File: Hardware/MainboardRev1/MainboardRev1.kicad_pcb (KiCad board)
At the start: 4 copper layers, 92 x 92 mm, 224 parts, among them J1 BACKUP_BATT: 1586038-2, J10 Switch_1, J11 Switch_3, J12 Switch_2, J13 Switch_4, J14 Buzzer, J15 Strobe, J2 MAIN_BATT: 1586038-2, J3 Servo_Control, J4 EMATCH_1: 1586038-2, J5 EMATCH_2: 1586038-2, J6 Stratologger_PWR: 1586038-2, J7 Stratologger_DATA, J8 U.FL-R-SMT-1(10), J9 0733910320 [915MHz SMA], Q1 SSM3J328R, Q10 SSM3J328R, Q11 NTR4003, Q12 NTR4003, Q13 NTR4003, Q14 NTR4003, Q15 SSM3J328R, Q16 NTR4003, Q17 SSM3J328R, Q18 SSM3J328R, Q19 NTR4003, Q2 SSM3J328R, Q20 NTR4003, Q21 SIS612EDNT-T1-GE3, Q22 SIS612EDNT-T1-GE3, Q23 NTR4003, Q24 NTR4003, Q25 NTR4003, Q26 SSM3J328R, Q27 NTR4003, Q28 SSM3J328R, Q29 SSM3J328R, Q3 SSM3J328R, Q30 NTR4003, Q31 NTR4003, Q4 SSM3J328R, Q5 NTR4003, Q6 NTR4003, Q7 NTR4003, Q8 SSM3J328R, Q9 NTR4003, SW1 EG2201A [DPDT], U1 LT6703-3, U10 LTC4358, U11 Teensy3.6, U12 ABPMANN030PG2A3, U13 LSM9DS1, U14 LIS331HH, U15 BME280, U16 CCS811, U17 ublox_max-m8q, U18 RFM69HCW, U2 LTC3605, U3 LTC4358, U4 LTC4358, U5 LDL1117S50R, U6 LDL1117S33R, U7 LTC2992, U8 LDL1117S33R, U9 LTC2992

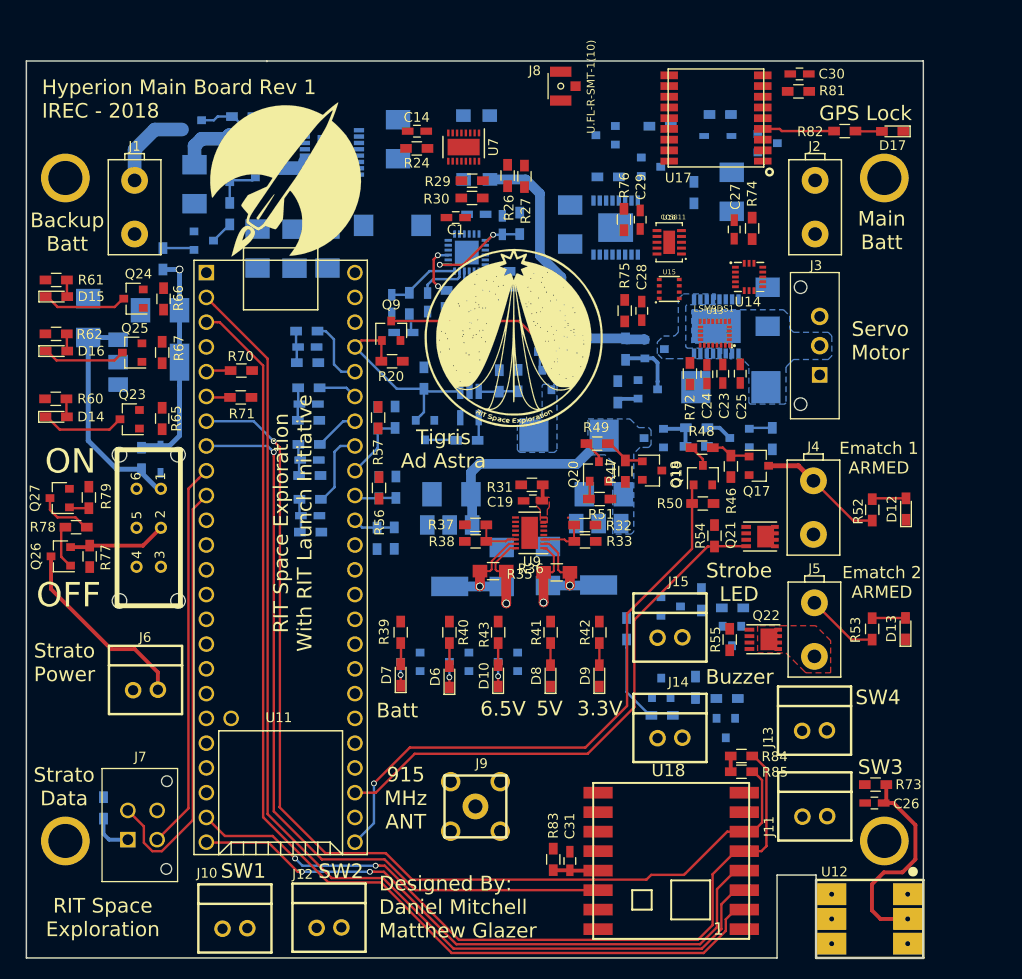
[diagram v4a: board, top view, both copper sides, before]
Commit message: committing progress, estimating the board is approx 1/3 routed
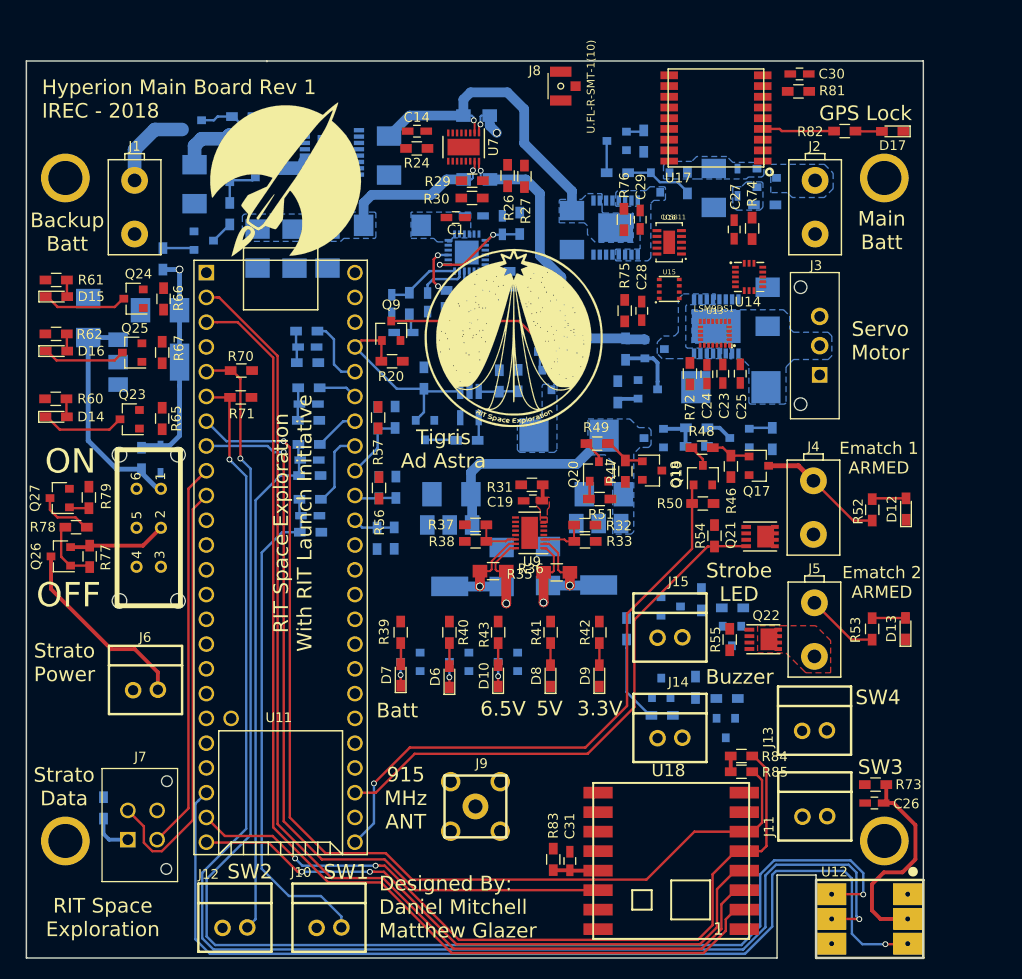
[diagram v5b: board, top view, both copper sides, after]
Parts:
- moved R2 10.3 mm to (125.7, 64.8)
- moved J10 9.65 mm to (81.0, 138.9)
- moved J12 9.65 mm to (71.4, 138.9)
- moved D2 5.16 mm to (122.9, 62.4), turned to 90 degrees
- moved Q2 3.56 mm to (125.9, 62.0)
- moved R13 2.27 mm to (113.3, 58.2), turned to 270 degrees
- moved C11 1.91 mm to (87.2, 59.7)
- moved C3 1.88 mm to (120.5, 63.0)
- moved Q4 1.86 mm to (115.0, 62.5), turned to 270 degrees
- moved Q6 1.28 mm to (110.5, 58.2)
- moved R8 1.22 mm to (117.8, 62.5)
- moved R11 1.04 mm to (110.6, 61.5)
- moved C13 0.59 mm to (106.0, 67.3)
- moved C6 0.31 mm to (95.9, 65.9)
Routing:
- net SENSORS_SCL: track 2.54 -> 143.8 mm, vias 0 -> 2
- net SENSORS_SDA: track 2.47 -> 142.9 mm, vias 0 -> 2
- net INT_PRESSURE: track 0.00 -> 102.3 mm, vias 0 -> 1
- net Net-(C34-Pad1): track 3.32 -> 53.0 mm
- net Net-(C32-Pad1): track 3.48 -> 52.1 mm
- net BATTERY_PWR_MSMT: track 0.00 -> 32.6 mm, vias 0 -> 1
- net +6.5V_MSMT: track 5.67 -> 22.9 mm, vias 2 -> 3
- net Net-(Q4-Pad1): track 0.00 -> 7.08 mm
- net BATTERY_PWR: track 0.00 -> 4.81 mm, vias 0 -> 2
- net Net-(Q6-Pad3): track 0.00 -> 3.27 mm
- net +6.5V: track 33.4 -> 36.2 mm, vias 0 -> 1
- net Net-(Q26-Pad1): track 4.62 -> 6.64 mm
- net MAIN_BATT_EN: track 0.00 -> 1.82 mm
- net COMMS_MISO: track 111.6 -> 112.7 mm
- net COMMS_MOSI: track 114.2 -> 114.9 mm
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- added copper zone on B.Cu, net +6.5V_MSMT
- added copper zone on B.Cu, net BATTERY_PWR_MSMT
- added copper zone on 3V3.Cu, net GND
- added copper zone on B.Cu, net MAIN_BATT
- added copper zone on B.Cu, net Net-(C6-Pad2)
- added copper zone on B.Cu, net Net-(D2-Pad2)
- added copper zone on B.Cu, net Net-(J2-Pad1)
- added copper zone on B.Cu, net Net-(Q4-Pad3)

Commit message: All routing except for the antenna connections is finished
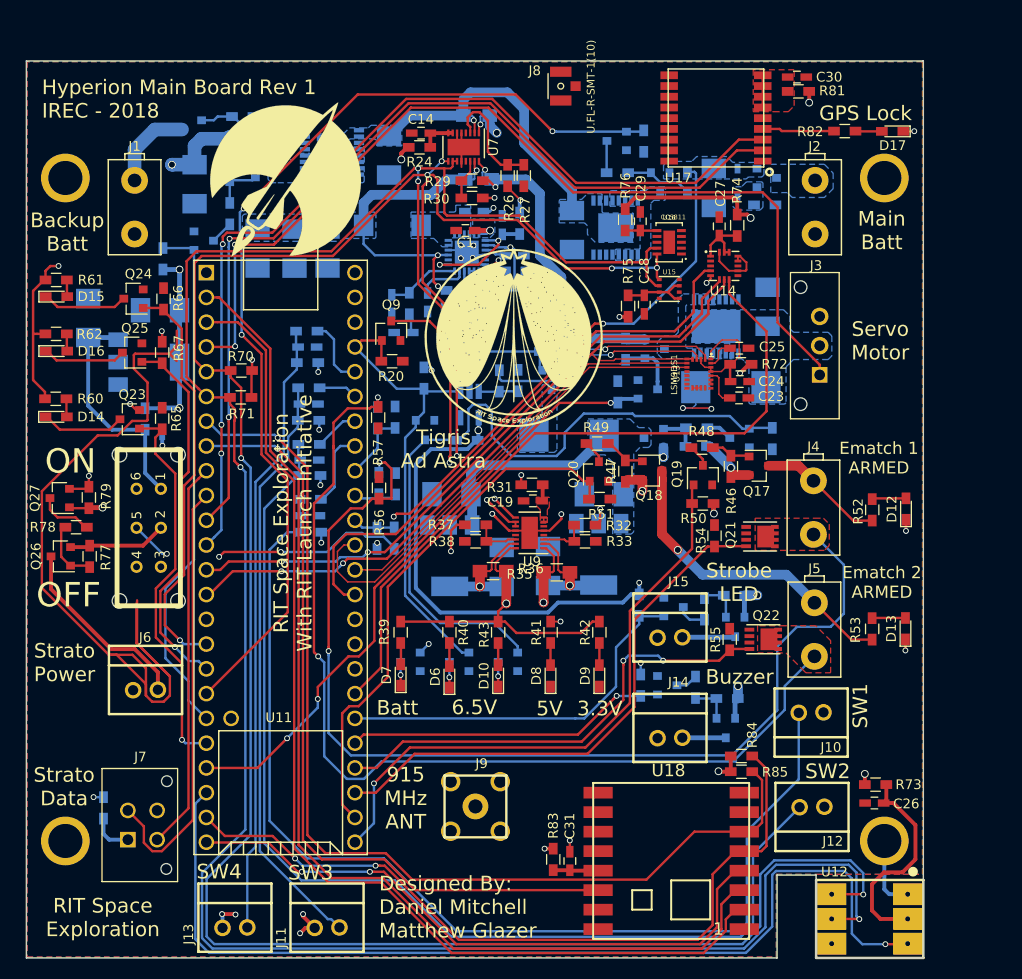
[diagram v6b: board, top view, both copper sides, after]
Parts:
- added C36: C_0603_HandSoldering, Capacitors_SMD:C_0603_HandSoldering, B.Cu at (100.1, 70.0)
- moved J13 62.8 mm to (71.4, 138.9)
- moved J12 60.5 mm to (130.6, 126.5), turned to 180 degrees
- moved J10 54.1 mm to (130.5, 116.9), turned to 180 degrees
- moved J11 51.3 mm to (80.8, 138.9)
- moved R72 5.31 mm to (123.3, 81.1), turned to 0 degrees
- moved U13 4.45 mm to (119.0, 82.1), turned to 270 degrees
- moved R34 4.07 mm to (62.2, 86.7)
- moved D5 3.86 mm to (63.9, 87.0)
- moved R98 3.79 mm to (113.0, 114.0), turned to 270 degrees
- moved C24 3.46 mm to (123.2, 82.9), turned to 0 degrees
- moved C23 2.99 mm to (123.1, 84.6), turned to 0 degrees
- moved U14 2.79 mm to (120.2, 70.0)
- moved R99 2.76 mm to (112.9, 105.8), turned to 270 degrees
- moved C25 2.61 mm to (123.1, 79.5), turned to 0 degrees
- moved C1 1.66 mm to (95.0, 67.4)
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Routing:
- net BATTERY_PWR: track 4.81 -> 133.2 mm, vias 2 -> 10
- net +5V: track 7.85 -> 132.7 mm, vias 1 -> 3
- net SENSORS_SDA: track 142.9 -> 264.0 mm, vias 2 -> 6
- net +3.3V_STARTUP: track 36.5 -> 150.8 mm, vias 1 -> 7
- net SENSORS_SCL: track 143.8 -> 257.1 mm, vias 2 -> 8
- net EMATCH_1_CHECK: track 0.00 -> 107.3 mm, vias 0 -> 2
- net MAIN_BATT_EN: track 1.82 -> 103.3 mm, vias 0 -> 3
- net EMATCH_2_CHECK: track 0.00 -> 101.0 mm, vias 0 -> 2
- net COMMS_TX: track 0.00 -> 99.0 mm, vias 0 -> 3
- net SERVO_PWM: track 0.00 -> 98.1 mm, vias 0 -> 2
- net COMMS_RX: track 0.00 -> 95.5 mm, vias 0 -> 2
- net (no net): track 0.00 -> 84.6 mm
- net SENSORS_MOSI: track 0.00 -> 78.5 mm, vias 0 -> 4
- net SENSORS_MISO: track 0.00 -> 78.3 mm, vias 0 -> 2
- net SENSORS_CS_LIS: track 0.00 -> 74.1 mm
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- added copper zone on GND.Cu, net +3.3V
- added copper zone on B.Cu, net BATTERY_PWR
- added copper zone on F.Cu, net EMATCH_1_CHECK
- added copper zone on B.Cu, net GND
- added copper zone on F.Cu, net GND
- added copper zone on F.Cu, net Net-(C30-Pad1)
- added copper zone on B.Cu, net Net-(Q3-Pad3)
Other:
- rule trace_min: 0.2 -> 0.15

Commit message: fixed trace width issues relating to the IMU, routed the antenna traces
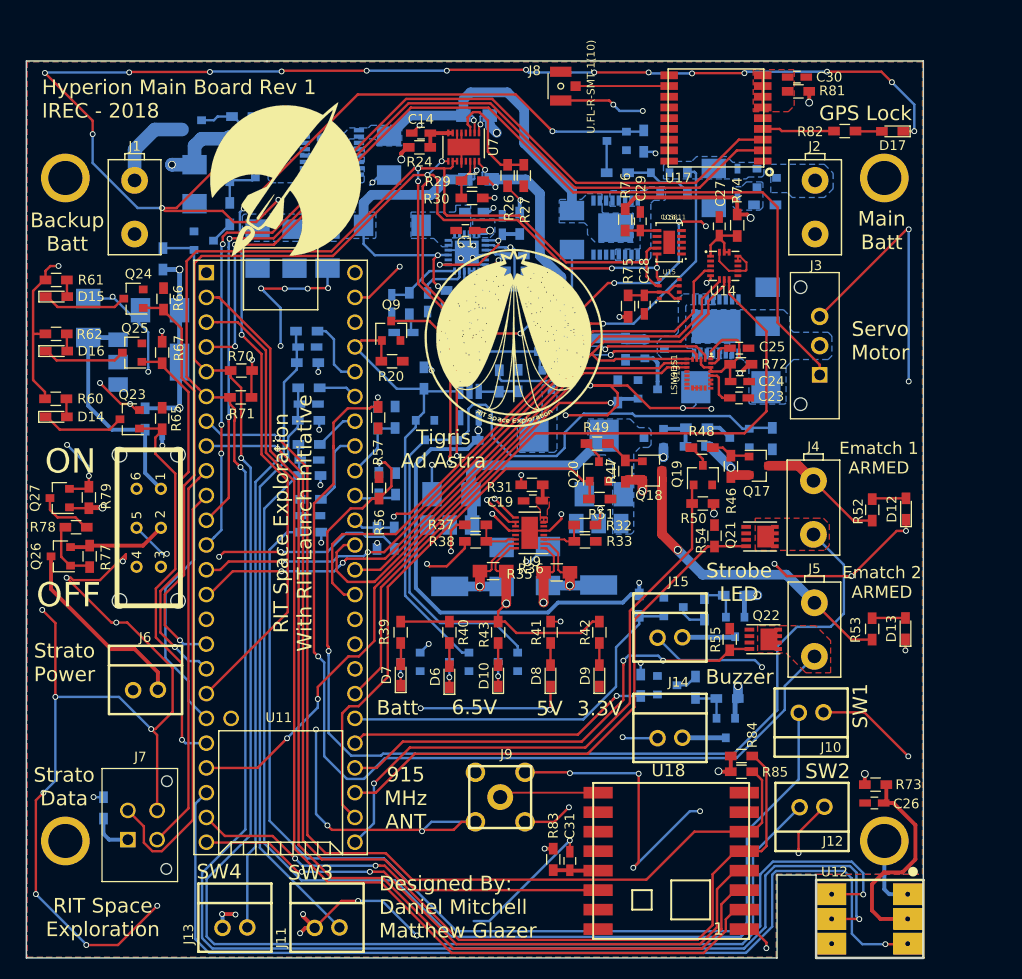
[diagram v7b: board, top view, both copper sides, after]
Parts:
- moved J9 2.72 mm to (98.6, 125.5)
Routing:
- net GND: track 75.0 -> 624.5 mm, vias 24 -> 98
- net (no net): track 84.6 -> 0.00 mm
- net Net-(J9-Pad1): track 0.00 -> 10.2 mm
- net Net-(J8-Pad1): track 0.00 -> 9.60 mm
- net SENSORS_CS_M: track 49.5 -> 50.3 mm
- net SENSORS_SCLK: track 73.5 -> 74.1 mm
- net EMATCH_1_CHECK: track 107.3 -> 106.7 mm
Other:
- net class Default: clearance 0.2 -> 0.15
- rule trace_clearance: 0.2 -> 0.15

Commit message: PCB updated per the DFM checks
via and trace width changes, changed to meet the requirments per the manufacturer's abilities
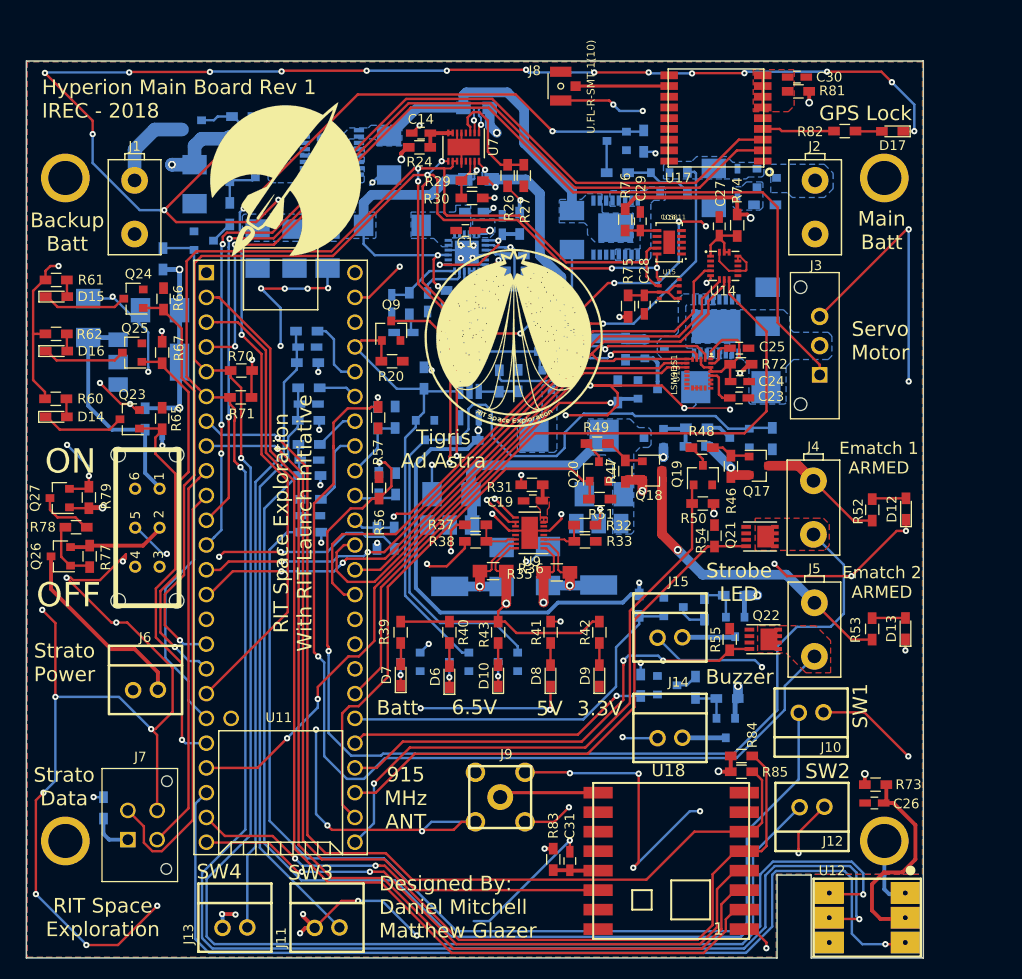
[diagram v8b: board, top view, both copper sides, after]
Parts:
- moved R25 0.79 mm to (96.2, 54.8)
- moved U12 0.28 mm to (136.2, 137.9)
- moved SW1 0.14 mm to (62.4, 97.9)
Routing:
- net BATTERY_PWR: track 133.2 -> 135.0 mm
- net GND: track 624.5 -> 626.2 mm
- net SENSORS_CS_M: track 50.3 -> 49.6 mm
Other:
- outline, holes or cut-outs redrawn
- net class Default: clearance 0.15 -> 0.16
- rule trace_clearance: 0.15 -> 0.16
- rule via_min_drill: 0.3 -> 0.25
